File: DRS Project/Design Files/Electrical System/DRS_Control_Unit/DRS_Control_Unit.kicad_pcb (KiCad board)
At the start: 2 copper layers, 30 parts, among them IC1 AP63301QWU-7, J1 Deutsch DT, J2 Screw, J3 Servo, U1 AMS1117, U2 Teensy4.0-NU-Teams, U3 TJA1051T-3

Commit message: more updates and sync
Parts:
- R5, R7: footprint Resistor_SMD:R_1206_3216Metric_Pad1.30x1.75mm_HandSolder -> Connector_PinSocket_2.54mm:PinSocket_1x02_P2.54mm_Vertical
- moved R1 126.8 mm to (127.0, 139.5), turned to -90 degrees
- moved U2 106.2 mm to (118.6, 112.4), turned to 180 degrees
- moved R7 102.1 mm to (131.0, 130.5)
- moved D4 94.3 mm to (122.5, 139.5), turned to 90 degrees
- moved D5 85.9 mm to (118.0, 132.5), turned to -90 degrees
- moved TP1 80.0 mm to (127.0, 124.5)
- moved TP2 73.9 mm to (122.0, 124.5)
- moved U3 73.0 mm to (124.5, 132.1)
- moved J3 72.8 mm to (89.0, 118.0)
- moved J1 59.6 mm to (62.9, 96.6), turned to 90 degrees
- moved R4 4.43 mm to (70.5, 138.5)
- moved U1 1.51 mm to (67.8, 133.0)
- moved C1 1.13 mm to (74.5, 129.5)
- moved D3 1.13 mm to (74.5, 135.0)
- moved C4 1.00 mm to (66.0, 127.5)
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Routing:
- net Net-(C3-Pad2): track 22.8 -> 0.00 mm
- net /FB: track 16.7 -> 0.00 mm
- net +12V: track 12.9 -> 0.00 mm
- net /VIN: track 9.93 -> 0.00 mm
- net Net-(IC1-SW): track 8.39 -> 0.00 mm
- net Net-(IC1-BST): track 3.92 -> 0.00 mm
- net Net-(D2-K): track 3.13 -> 0.00 mm
- net Net-(D1-K): track 2.93 -> 0.00 mm
- net Net-(C5-Pad2): track 1.88 -> 0.00 mm
- net GND: track 1.80 -> 0.00 mm

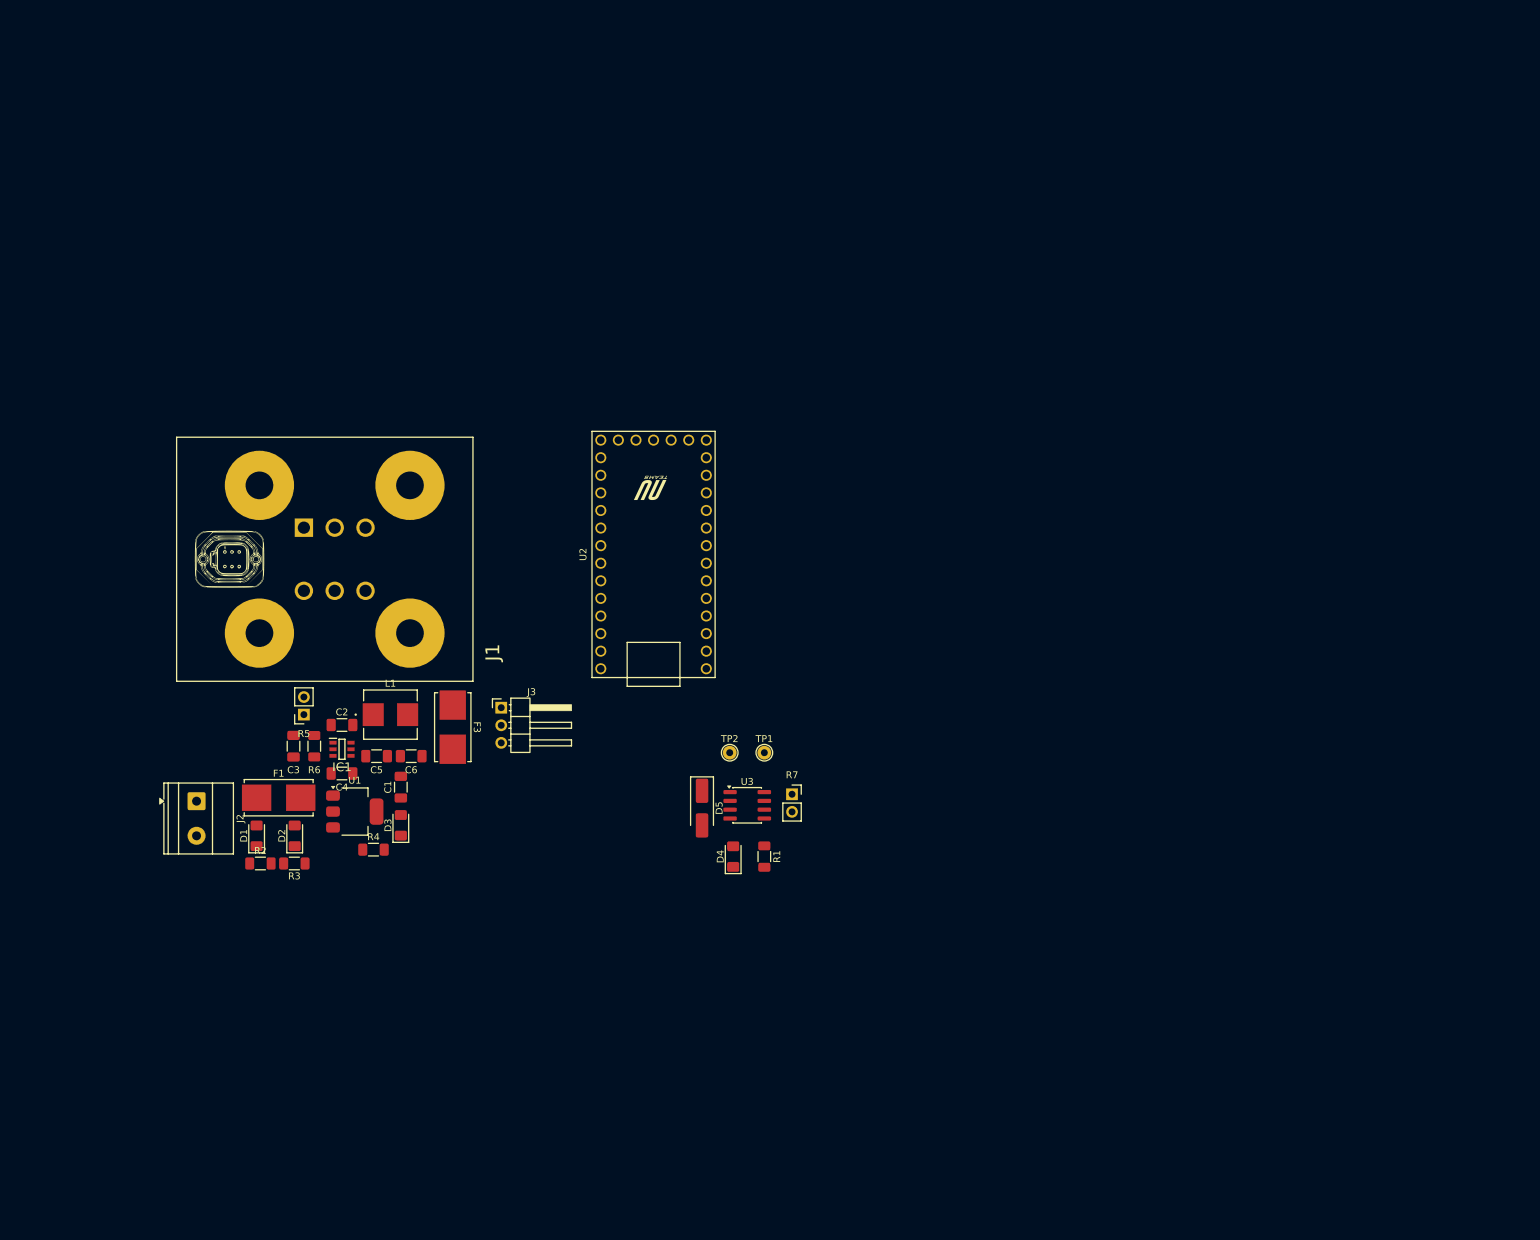
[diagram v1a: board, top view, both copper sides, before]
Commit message: added mounting and edgecut layer to pcb
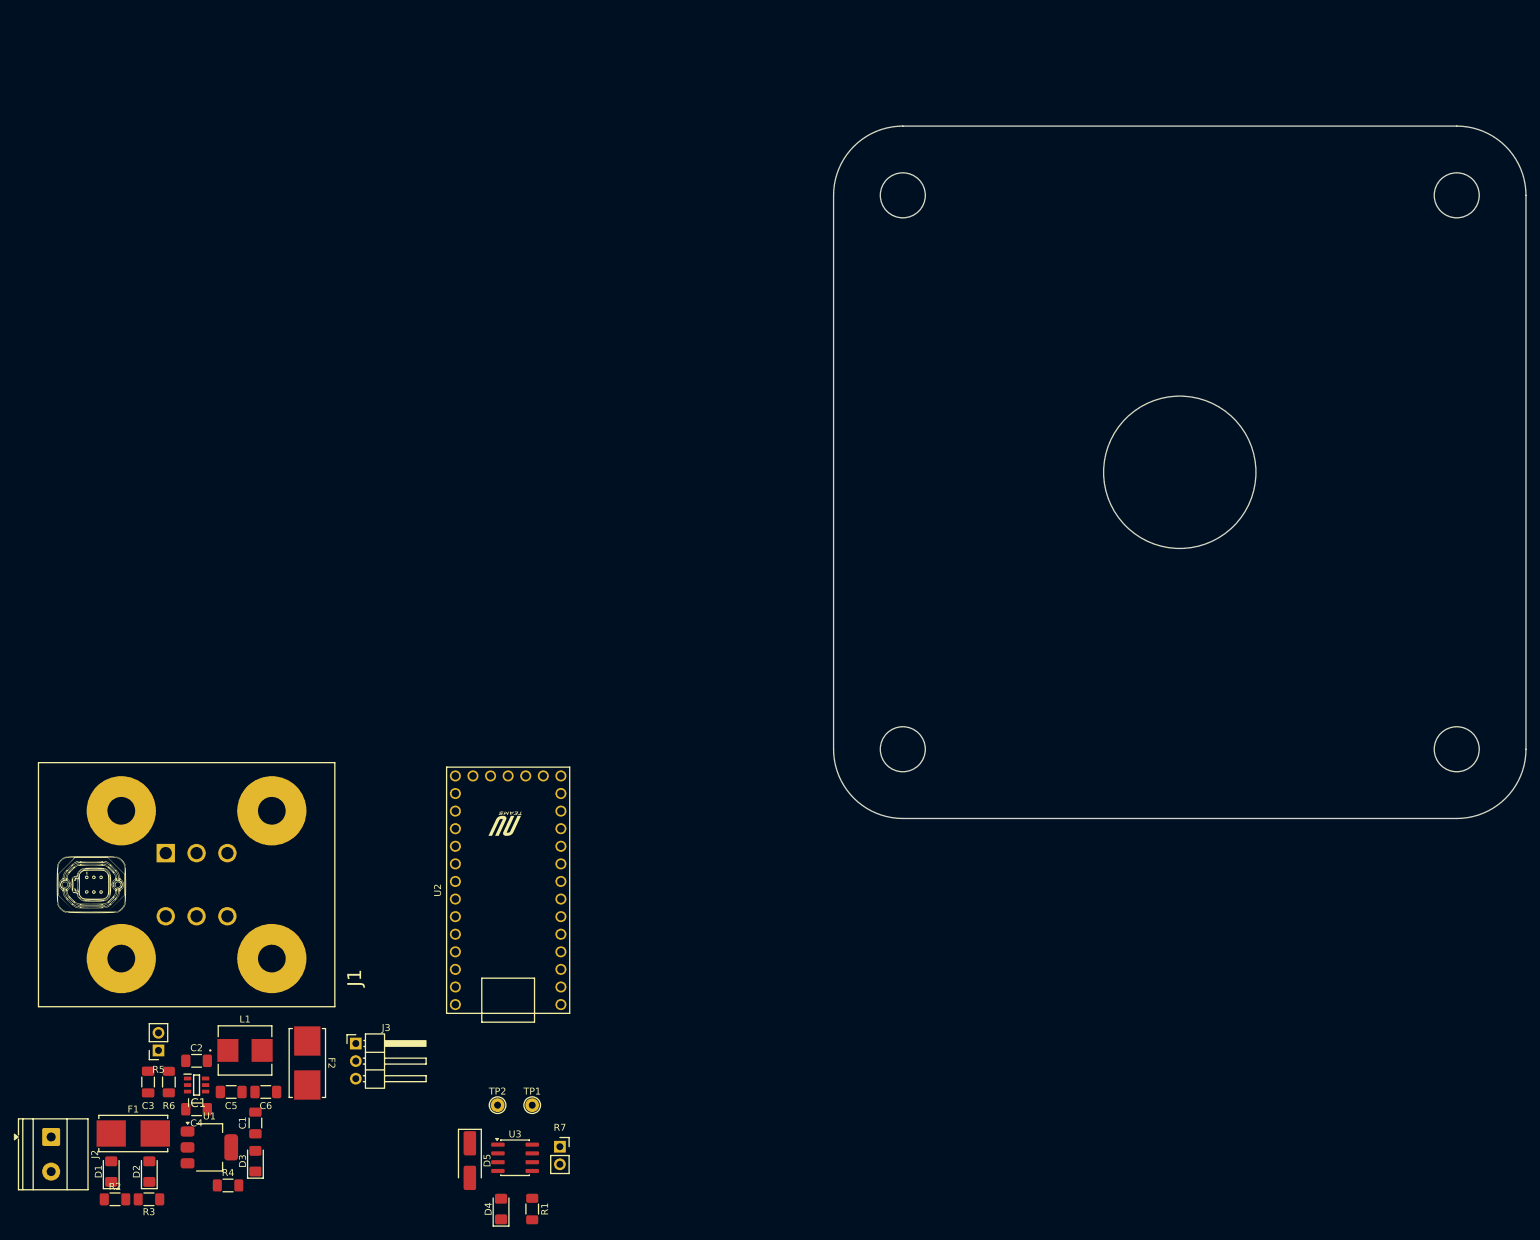
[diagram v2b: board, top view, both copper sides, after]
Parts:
- added REF**: MountingHole_6.5mm, MountingHole:MountingHole_6.5mm, F.Cu at (147.0, 124.0)
- added REF**: MountingHole_6.5mm, MountingHole:MountingHole_6.5mm, F.Cu at (227.0, 44.0)
- added REF**: MountingHole_6.5mm, MountingHole:MountingHole_6.5mm, F.Cu at (227.0, 124.0)
- added REF**: MountingHole_6.5mm, MountingHole:MountingHole_6.5mm, F.Cu at (147.0, 44.0)
- moved D4 61.0 mm to (89.0, 190.4)
- moved D5 61.0 mm to (84.5, 183.4)
- moved R1 61.0 mm to (93.5, 190.4)
- moved R7 61.0 mm to (97.5, 181.4)
- moved TP1 61.0 mm to (93.5, 175.4)
- moved TP2 61.0 mm to (88.5, 175.4)
- moved U3 61.0 mm to (91.0, 183.0)
- moved C1 52.9 mm to (53.5, 178.0)
- moved C2 52.9 mm to (45.0, 169.0)
- moved C3 52.9 mm to (38.0, 172.1)
- moved C4 52.9 mm to (45.0, 176.0)
- moved C5 52.9 mm to (50.0, 173.5)
- moved C6 52.9 mm to (55.0, 173.5)
- moved D1 52.9 mm to (32.7, 185.0)
- moved D2 52.9 mm to (38.2, 185.0)
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- renumbered F3 to F2
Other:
- board outline added: 100 x 100 mm
